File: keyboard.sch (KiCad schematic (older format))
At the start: 67 parts, among them SW10 S, SW11 Z, SW12 Frac, SW13 SK2, SW14 3, SW15 E, SW16 D, SW17 X, SW18 Root, SW19 SK3, SW2 1, SW20 4, SW21 R, SW22 F, SW23 C, SW24 Exp, SW25 SK4, SW26 5, SW27 T, SW28 G, SW29 V, SW3 Q, SW30 Spc, SW31 SK5, SW32 6, SW33 Y, SW34 H, SW35 B, SW36 ,, SW37 SK6, SW38 7, SW39 U, SW4 A, SW40 J, SW41 N, SW42 ., SW43 SK7, SW44 8, SW45 I, SW46 K, SW47 Down, SW48 M, SW49 SK8, SW5 Shft, SW50 9, SW51 O, SW52 L, SW53 Entr, SW54 Left, SW55 SK9, SW56 0, SW57 P, SW58 Bksp, SW59 Up, SW6 Sym, SW60 Right, SW61 SK10, SW7 SK1, SW8 2, SW9 W

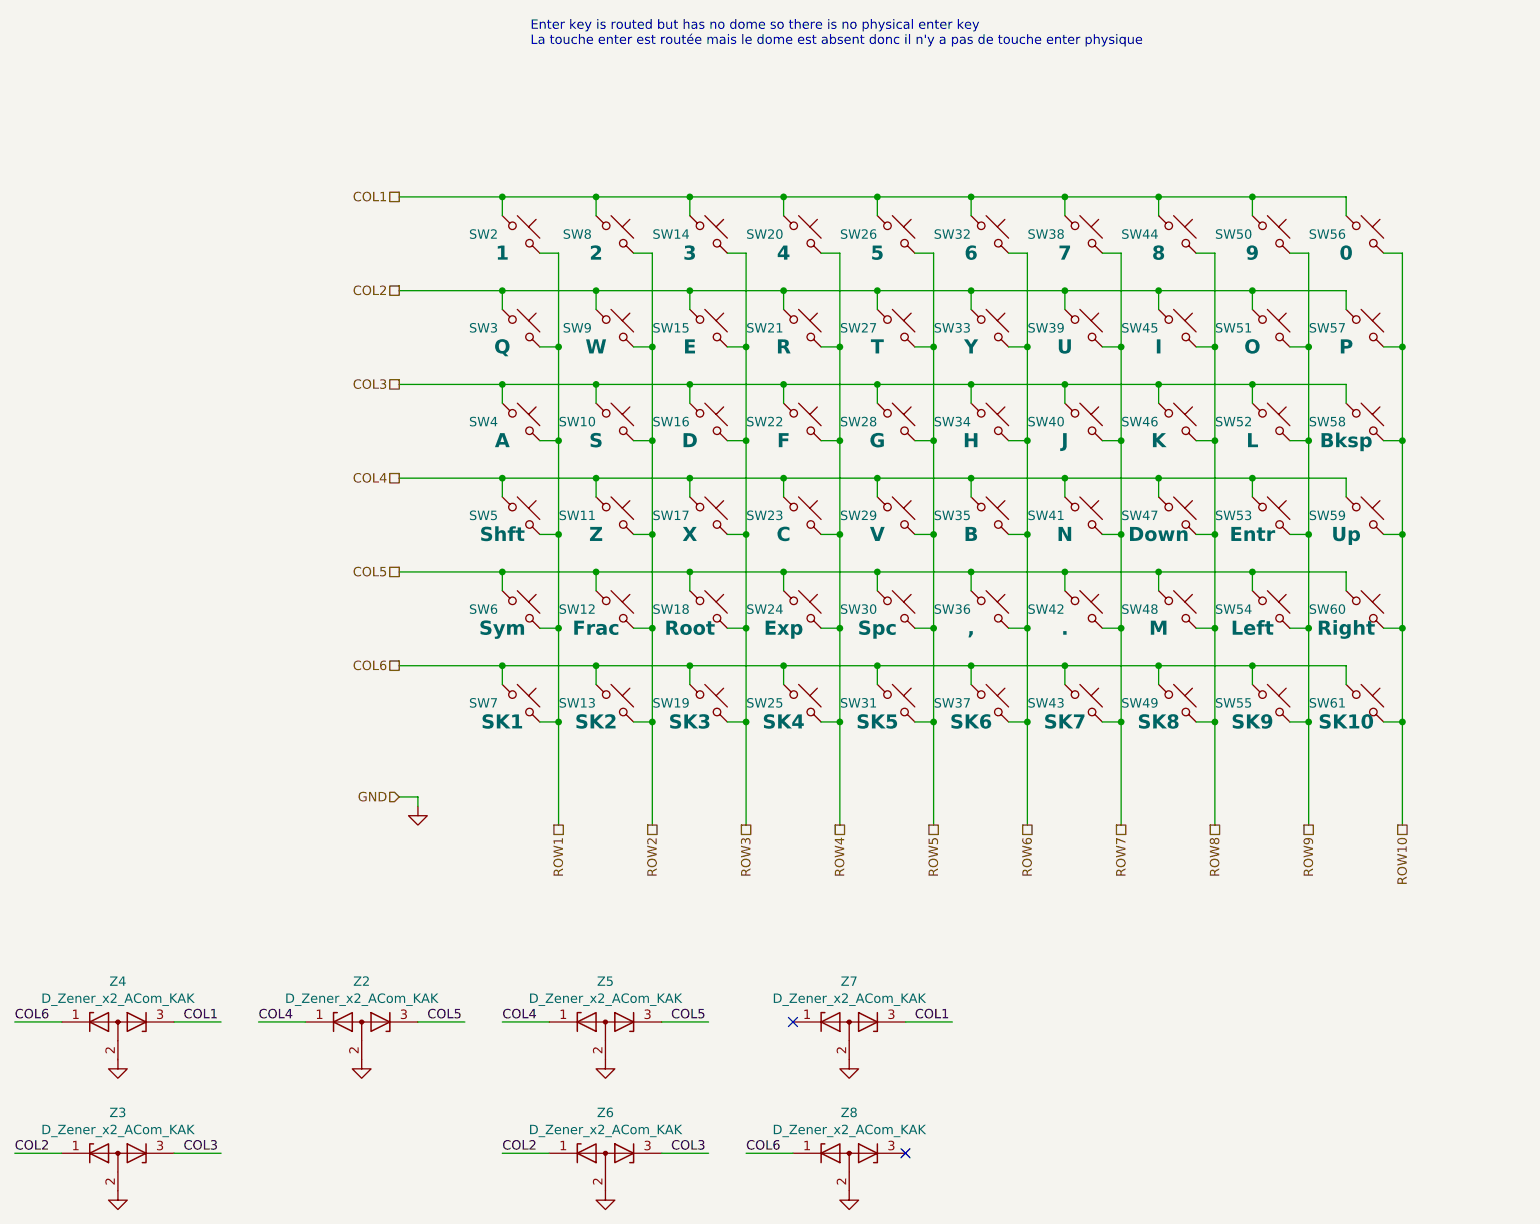
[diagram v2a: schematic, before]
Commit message: Fill in more missing components
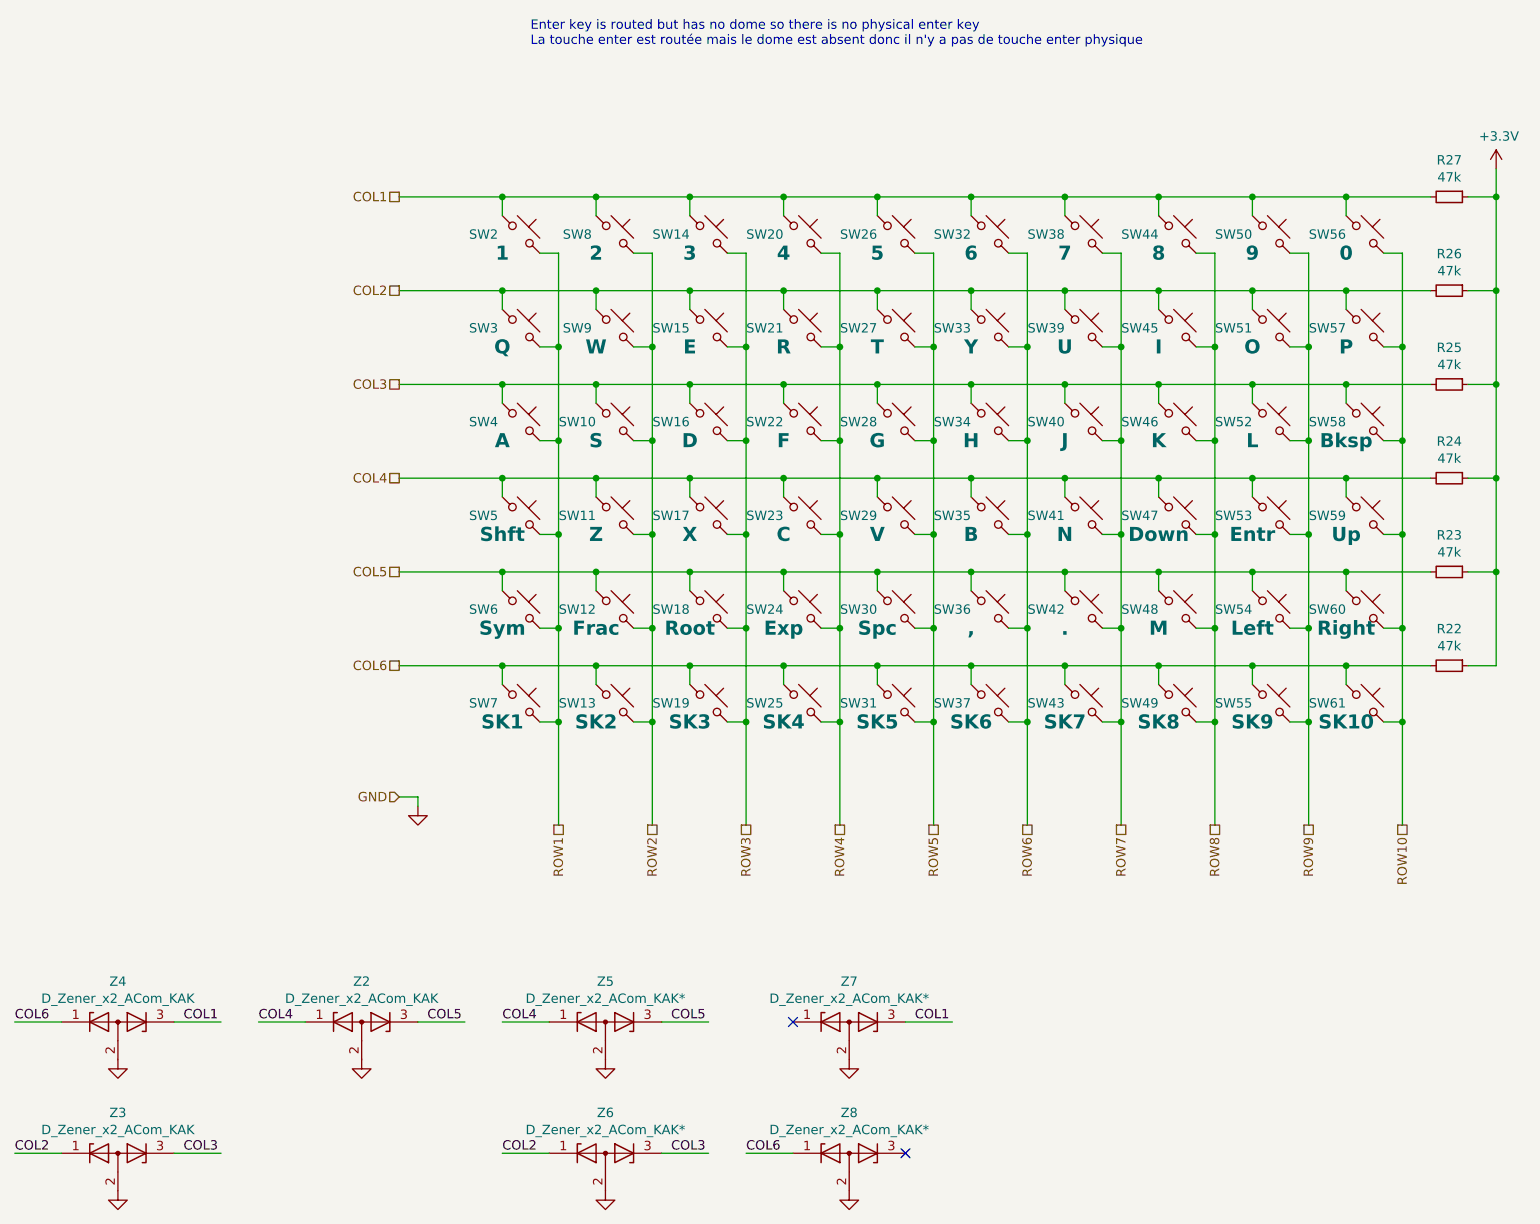
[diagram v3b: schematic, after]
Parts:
- added R22, R23, R24, R25, R26, R27: 47k, symbol Device:R_Small
- Z5, Z6, Z7, Z8: value D_Zener_x2_ACom_KAK -> D_Zener_x2_ACom_KAK*
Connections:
- net labels added: +3.3V
- wire segments 254 -> 272
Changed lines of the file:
@@
 Sheet 2 3
 Title "SMART Response XE - Keyboard"
-Date "2019-11-03"
+Date "2021-09-09"
 Rev "1.0"
 Comp ""
@@
 P 4100 6350
 F 0 "Z5" H 4100 6566 50  0000 C CNN
-F 1 "D_Zener_x2_ACom_KAK" H 4100 6475 50  0000 C CNN
+F 1 "D_Zener_x2_ACom_KAK*" H 4100 6475 50  0000 C CNN
 F 2 "" H 4100 6350 50  0001 C CNN
 F 3 "~" H 4100 6350 50  0001 C CNN
@@
 P 4100 7050
 F 0 "Z6" H 4100 7266 50  0000 C CNN
-F 1 "D_Zener_x2_ACom_KAK" H 4100 7175 50  0000 C CNN
+F 1 "D_Zener_x2_ACom_KAK*" H 4100 7175 50  0000 C CNN
 F 2 "" H 4100 7050 50  0001 C CNN
 F 3 "~" H 4100 7050 50  0001 C CNN
@@
 P 5400 6350
 F 0 "Z7" H 5400 6566 50  0000 C CNN
-F 1 "D_Zener_x2_ACom_KAK" H 5400 6475 50  0000 C CNN
+F 1 "D_Zener_x2_ACom_KAK*" H 5400 6475 50  0000 C CNN
 F 2 "" H 5400 6350 50  0001 C CNN
 F 3 "~" H 5400 6350 50  0001 C CNN
@@
 P 5400 7050
 F 0 "Z8" H 5400 7266 50  0000 C CNN
-F 1 "D_Zener_x2_ACom_KAK" H 5400 7175 50  0000 C CNN
+F 1 "D_Zener_x2_ACom_KAK*" H 5400 7175 50  0000 C CNN
 F 2 "" H 5400 7050 50  0001 C CNN
 F 3 "~" H 5400 7050 50  0001 C CNN
@@
 Text Notes 3700 1150 0    50   ~ 0
 Enter key is routed but has no dome so there is no physical enter key\nLa touche enter est routée mais le dome est absent donc il n'y a pas de touche enter physique
+$Comp
+L Device:R_Small R26
+U 1 1 6409FC0F
+P 8600 2450
+F 0 "R26" V 8404 2450 50  0000 C CNN
+F 1 "47k" V 8495 2450 50  0000 C CNN
+F 2 "" H 8600 2450 50  0001 C CNN
+F 3 "~" H 8600 2450 50  0001 C CNN
+	1    8600 2450
+	0    1    1    0
+$EndComp
+$Comp
+L power:+3.3V #PWR02
+U 1 1 640A0FFB
+P 8850 1800
+F 0 "#PWR02" H 8850 1650 50  0001 C CNN
+F 1 "+3.3V" H 8865 1973 50  0000 C CNN
+F 2 "" H 8850 1800 50  0001 C CNN
+F 3 "" H 8850 1800 50  0001 C CNN
+	1    8850 1800
+	1    0    0    -1
+$EndComp
+$Comp
+L Device:R_Small R27
+U 1 1 64155AD6
+P 8600 1950
+F 0 "R27" V 8404 1950 50  0000 C CNN
+F 1 "47k" V 8495 1950 50  0000 C CNN
+F 2 "" H 8600 1950 50  0001 C CNN
+F 3 "~" H 8600 1950 50  0001 C CNN
+	1    8600 1950
+	0    1    1    0
+$EndComp
+Wire Wire Line
+	8050 1950 8500 1950
+Connection ~ 8050 1950
+Wire Wire Line
+	8700 1950 8850 1950
+Wire Wire Line
+	8850 1950 8850 1800
+$Comp
+L Device:R_Small R25
+U 1 1 6418A062
+P 8600 2950
+F 0 "R25" V 8404 2950 50  0000 C CNN
+F 1 "47k" V 8495 2950 50  0000 C CNN
+F 2 "" H 8600 2950 50  0001 C CNN
+F 3 "~" H 8600 2950 50  0001 C CNN
+	1    8600 2950
+	0    1    1    0
+$EndComp
+$Comp
+L Device:R_Small R24
+U 1 1 6419B3AB
+P 8600 3450
+F 0 "R24" V 8404 3450 50  0000 C CNN
+F 1 "47k" V 8495 3450 50  0000 C CNN
+F 2 "" H 8600 3450 50  0001 C CNN
+F 3 "~" H 8600 3450 50  0001 C CNN
+	1    8600 3450
+	0    1    1    0
+$EndComp
+$Comp
+L Device:R_Small R23
+U 1 1 641AC6D4
+P 8600 3950
+F 0 "R23" V 8404 3950 50  0000 C CNN
+F 1 "47k" V 8495 3950 50  0000 C CNN
+F 2 "" H 8600 3950 50  0001 C CNN
+F 3 "~" H 8600 3950 50  0001 C CNN
+	1    8600 3950
+	0    1    1    0
+$EndComp
+$Comp
+L Device:R_Small R22
+U 1 1 641BD9A5
+P 8600 4450
+F 0 "R22" V 8404 4450 50  0000 C CNN
+F 1 "47k" V 8495 4450 50  0000 C CNN
+F 2 "" H 8600 4450 50  0001 C CNN
+F 3 "~" H 8600 4450 50  0001 C CNN
+	1    8600 4450
+	0    1    1    0
+$EndComp
+Wire Wire Line
+	8050 2450 8500 2450
+Connection ~ 8050 2450
+Wire Wire Line
+	8050 2950 8500 2950
+Connection ~ 8050 2950
+Wire Wire Line
+	8050 3450 8500 3450
+Connection ~ 8050 3450
+Wire Wire Line
+	8050 3950 8500 3950
+Connection ~ 8050 3950
+Wire Wire Line
+	8050 4450 8500 4450
+Connection ~ 8050 4450
+Wire Wire Line
+	8700 4450 8850 4450
+Wire Wire Line
+	8850 4450 8850 3950
+Connection ~ 8850 1950
+Wire Wire Line
+	8700 2450 8850 2450
+Connection ~ 8850 2450
+Wire Wire Line
+	8850 2450 8850 1950
+Wire Wire Line
+	8700 2950 8850 2950
+Connection ~ 8850 2950
+Wire Wire Line
+	8850 2950 8850 2450
+Wire Wire Line
+	8700 3450 8850 3450
+Connection ~ 8850 3450
+Wire Wire Line
+	8850 3450 8850 2950
+Wire Wire Line
+	8700 3950 8850 3950
+Connection ~ 8850 3950
+Wire Wire Line
+	8850 3950 8850 3450
 $EndSCHEMATC
